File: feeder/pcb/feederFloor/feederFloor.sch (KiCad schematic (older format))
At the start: 5 parts, among them J1 IDC, J2 Conn_01x10_Female, U1 DS2431

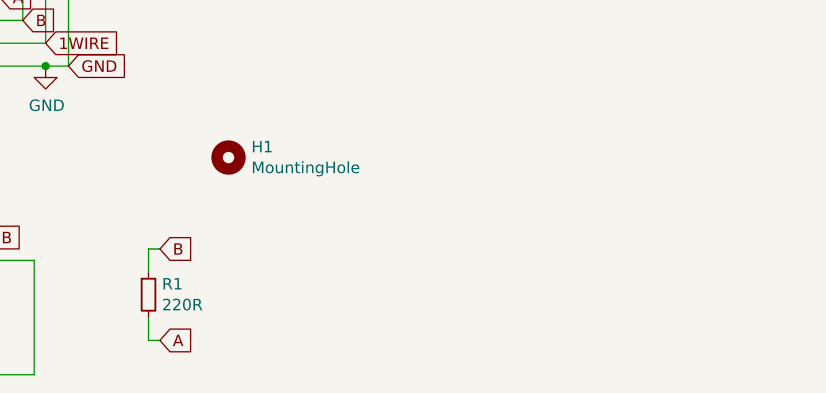
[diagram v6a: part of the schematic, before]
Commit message: Updating the value for R1 to the value suggested in the application note. Adding part numbers for the various sources (Digikey, Mouser, LCSC).
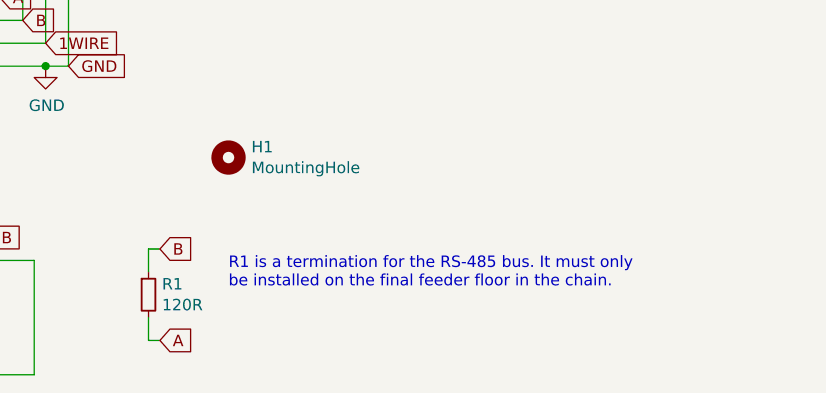
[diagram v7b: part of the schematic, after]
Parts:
- J1: Digikey (none) -> 732-5394-ND; LCSC (none) -> C601936; Mouser (none) -> 710-61200621621
- J2: Digikey (none) -> 70AAJ-5-F0GCT-ND; Mouser (none) -> 652-70AAJ-5-F0G
- R1: value 220R -> 120R; Digikey (none) -> RMCF0805JT120RCT-ND; JLCPCB C17557 -> C17437; LCSC (none) -> C61683; Mouser (none) -> 652-CR0805FX-1200ELF
- U1: Digikey (none) -> DS2431P+T&RCT-ND; LCSC (none) -> C9387; Mouser (none) -> 700-DS2431PT&R
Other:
- note added: "R1 is a termination for the RS-485 bus. It must only \nbe installed on the final feeder floor in the chain."
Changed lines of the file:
@@
 F 2 "index:70AA-5" H 5600 1750 50  0001 C CNN
 F 3 "~" H 5600 1750 50  0001 C CNN
+F 4 "70AAJ-5-F0GCT-ND" V 5600 1750 50  0001 C CNN "Digikey"
+F 5 "652-70AAJ-5-F0G" V 5600 1750 50  0001 C CNN "Mouser"
 	1    5600 1750
 	0    -1   -1   0
@@
 F 2 "Package_SO_J-Lead:TSOC-6_3.76x3.94mm_P1.27mm" H 4700 1800 50  0001 C CNN
 F 3 "http://pdfserv.maximintegrated.com/en/ds/DS2401.pdf" H 3500 2400 50  0001 C CNN
+F 4 "700-DS2431PT&R" H 3650 2150 50  0001 C CNN "Mouser"
+F 5 "C9387" H 3650 2150 50  0001 C CNN "LCSC"
+F 6 "DS2431P+T&RCT-ND" H 3650 2150 50  0001 C CNN "Digikey"
 	1    3650 2150
 	1    0    0    -1
@@
 F 2 "Connector_IDC:IDC-Header_2x03_P2.54mm_Vertical" H 5550 3300 50  0001 C CNN
 F 3 "~" H 5550 3300 50  0001 C CNN
+F 4 "732-5394-ND" H 5550 3300 50  0001 C CNN "Digikey"
+F 5 "710-61200621621" H 5550 3300 50  0001 C CNN "Mouser"
+F 6 "C601936" H 5550 3300 50  0001 C CNN "LCSC"
 	1    5550 3300
 	-1   0    0    1
@@
 P 6450 3450
 F 0 "R1" H 6509 3496 50  0000 L CNN
-F 1 "220R" H 6509 3405 50  0000 L CNN
+F 1 "120R" H 6509 3405 50  0000 L CNN
 F 2 "Resistor_SMD:R_0805_2012Metric" H 6450 3450 50  0001 C CNN
 F 3 "~" H 6450 3450 50  0001 C CNN
-F 4 "C17557" H 6450 3450 50  0001 C CNN "JLCPCB"
+F 4 "C17437" H 6450 3450 50  0001 C CNN "JLCPCB"
+F 5 "C61683" H 6450 3450 50  0001 C CNN "LCSC"
+F 6 "RMCF0805JT120RCT-ND" H 6450 3450 50  0001 C CNN "Digikey"
+F 7 "652-CR0805FX-1200ELF" H 6450 3450 50  0001 C CNN "Mouser"
 	1    6450 3450
 	1    0    0    -1
@@
 Wire Wire Line
 	6450 3650 6500 3650
+Text Notes 6800 3425 0    50   ~ 0
+R1 is a termination for the RS-485 bus. It must only \nbe installed on the final feeder floor in the chain.
 $EndSCHEMATC

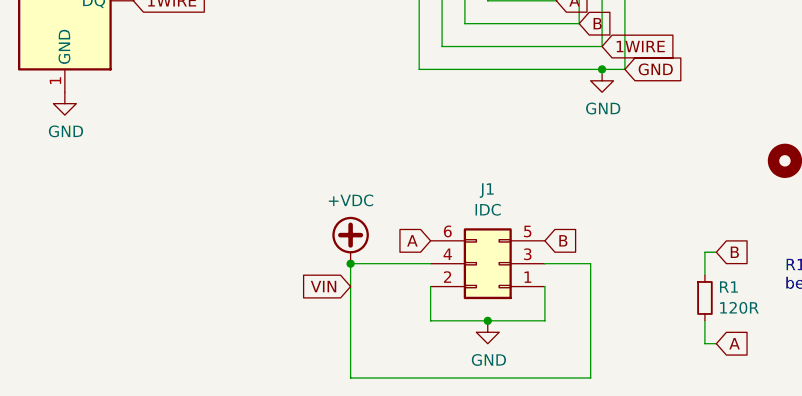
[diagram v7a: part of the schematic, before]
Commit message: Fixing some issues with the ERC and DRC to achieve a clean ERC & DRC build.
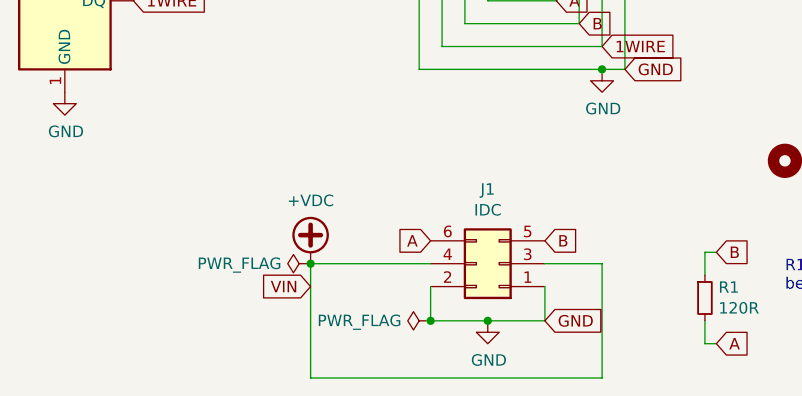
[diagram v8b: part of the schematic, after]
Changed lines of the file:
@@
 L power:+VDC #PWR0104
 U 1 1 6015A417
-P 4900 3300
-F 0 "#PWR0104" H 4900 3200 50  0001 C CNN
-F 1 "+VDC" H 4900 3575 50  0000 C CNN
-F 2 "" H 4900 3300 50  0001 C CNN
-F 3 "" H 4900 3300 50  0001 C CNN
-	1    4900 3300
+P 4725 3300
+F 0 "#PWR0104" H 4725 3200 50  0001 C CNN
+F 1 "+VDC" H 4725 3575 50  0000 C CNN
+F 2 "" H 4725 3300 50  0001 C CNN
+F 3 "" H 4725 3300 50  0001 C CNN
+	1    4725 3300
 	1    0    0    -1
 $EndComp
 Wire Wire Line
-	4900 3300 5250 3300
+	4725 3300 5250 3300
 Wire Wire Line
-	4900 3800 5950 3800
+	4725 3800 6000 3800
 Wire Wire Line
-	5950 3800 5950 3300
+	6000 3800 6000 3300
 Wire Wire Line
-	5950 3300 5750 3300
+	6000 3300 5750 3300
 Wire Wire Line
-	4900 3300 4900 3800
-Connection ~ 4900 3300
+	4725 3300 4725 3800
+Connection ~ 4725 3300
 Text GLabel 5250 3200 0    50   Input ~ 0
 A
@@
 Text GLabel 6000 2350 2    50   Input ~ 0
 1WIRE
-Text GLabel 4900 3400 0    50   Input ~ 0
+Text GLabel 4725 3400 0    50   Input ~ 0
 VIN
 $Comp
@@
 Text Notes 6800 3425 0    50   ~ 0
 R1 is a termination for the RS-485 bus. It must only \nbe installed on the final feeder floor in the chain.
+$Comp
+L power:PWR_FLAG #FLG0101
+U 1 1 603B4DA0
+P 4725 3300
+F 0 "#FLG0101" H 4725 3375 50  0001 C CNN
+F 1 "PWR_FLAG" V 4725 3427 50  0000 L CNN
+F 2 "" H 4725 3300 50  0001 C CNN
+F 3 "~" H 4725 3300 50  0001 C CNN
+	1    4725 3300
+	0    -1   -1   0
+$EndComp
+$Comp
+L power:PWR_FLAG #FLG0102
+U 1 1 603B607C
+P 5250 3550
+F 0 "#FLG0102" H 5250 3625 50  0001 C CNN
+F 1 "PWR_FLAG" V 5250 3677 50  0000 L CNN
+F 2 "" H 5250 3550 50  0001 C CNN
+F 3 "~" H 5250 3550 50  0001 C CNN
+	1    5250 3550
+	0    -1   -1   0
+$EndComp
+Connection ~ 5250 3550
+Text GLabel 5750 3550 2    50   Input ~ 0
+GND
 $EndSCHEMATC
